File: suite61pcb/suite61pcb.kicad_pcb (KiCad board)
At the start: 2 copper layers, 176.3 x 113.1 mm, 99 parts, among them J1 Battery JST, J2 OLED, J3 FFC_Receiver, SW1 MX_SW_HS, SW10 MX_SW_HS, SW11 MX_SW_HS, SW12 MX_SW_HS, SW13 MX_SW, SW14 MX_SW, SW15 MX_SW_HS, SW16 MX_SW_HS, SW17 MX_SW_HS, SW18 MX_SW_HS, SW19 MX_SW_HS, SW2 MX_SW_HS, SW20 Reset_Button, SW21 MX_SW, SW22 MX_SW, SW23 MX_SW_HS, SW24 MX_SW_HS, SW25 MX_SW_HS, SW26 MX_SW_HS, SW27 MX_SW_HS, SW28 MX_SW_HS, SW29 MX_SW_HS, SW3 MX_SW_HS, SW30 MX_SW_HS, SW31 MX_SW_HS, SW32 MX_SW_HS, SW33 MX_SW_HS, SW34 MX_SW_HS, SW35 MX_SW_HS, SW36 MX_SW_HS, SW37 RotaryEncoder_Switch, SW4 MX_SW_HS, SW5 MX_SW_HS, SW6 MX_SW_HS, SW7 MX_SW_HS, SW8 MX_SW_HS, SW9 MX_SW_HS, U1 nice_nano

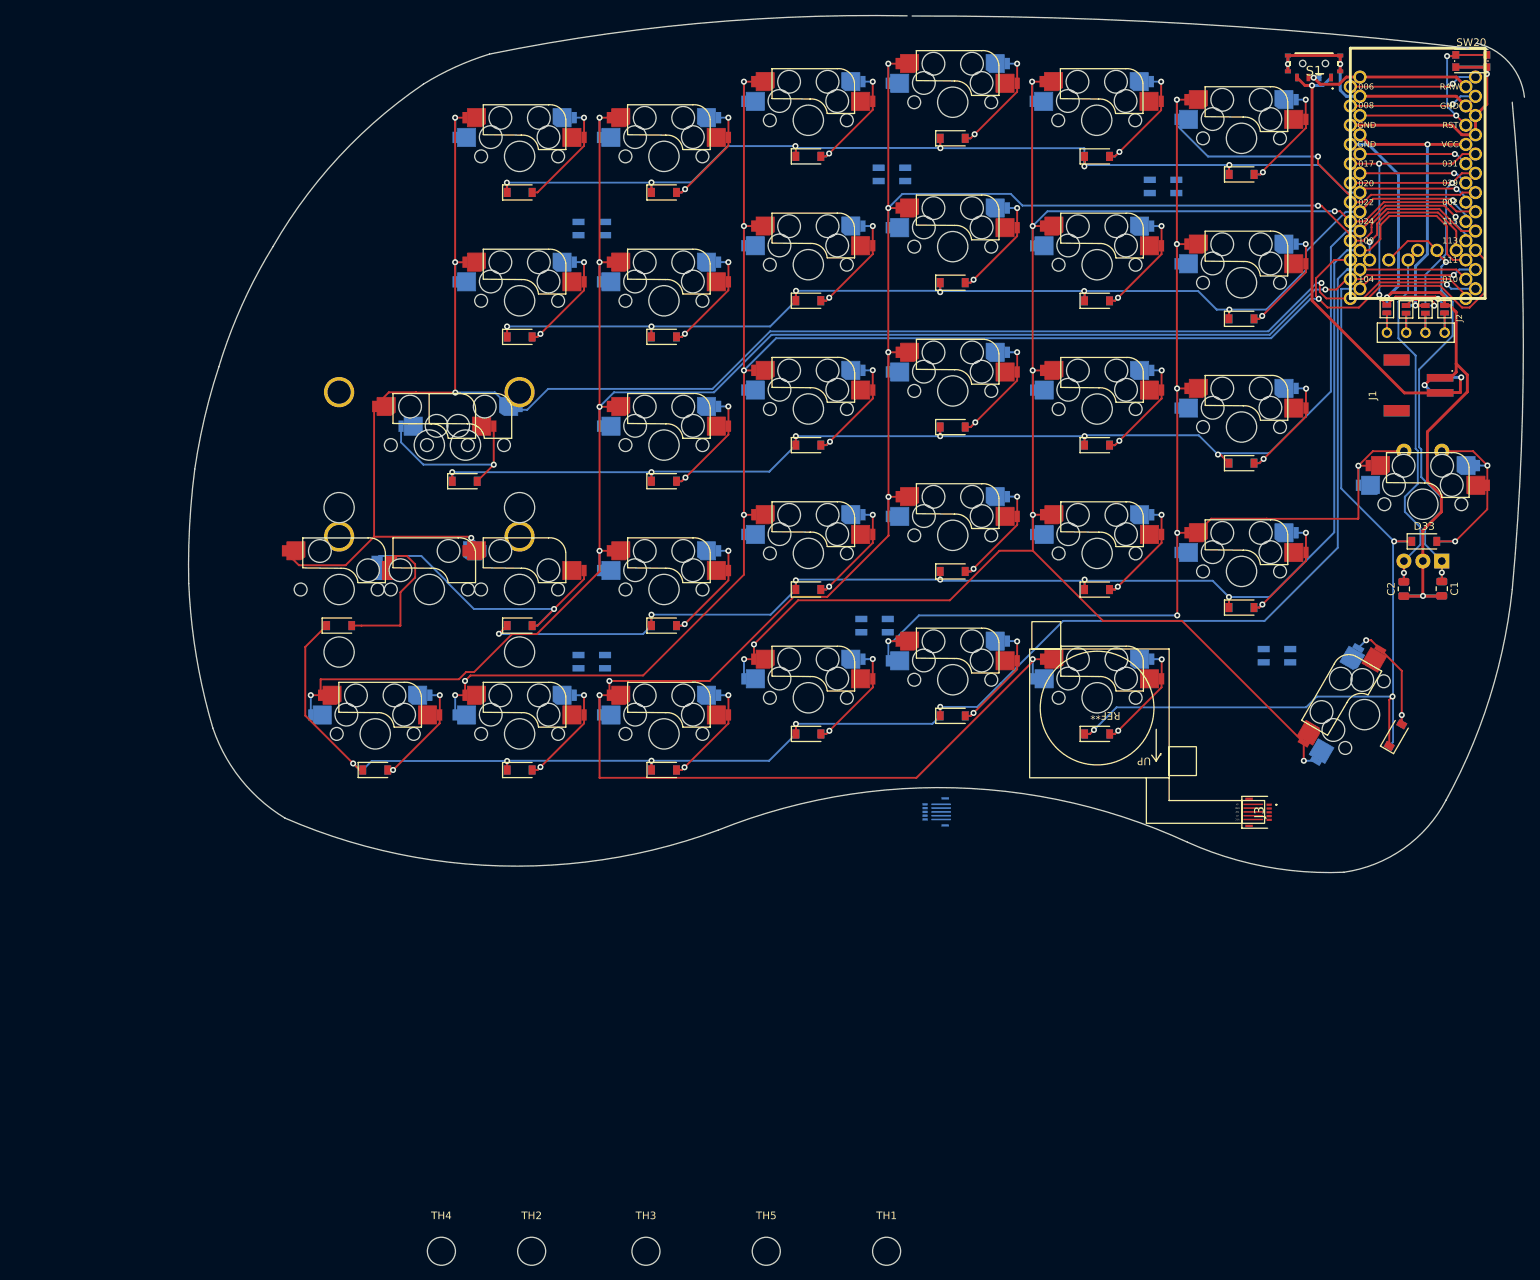
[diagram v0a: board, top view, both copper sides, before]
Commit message: finished routing pcb, look into possible trrs + magnetic connection between halves
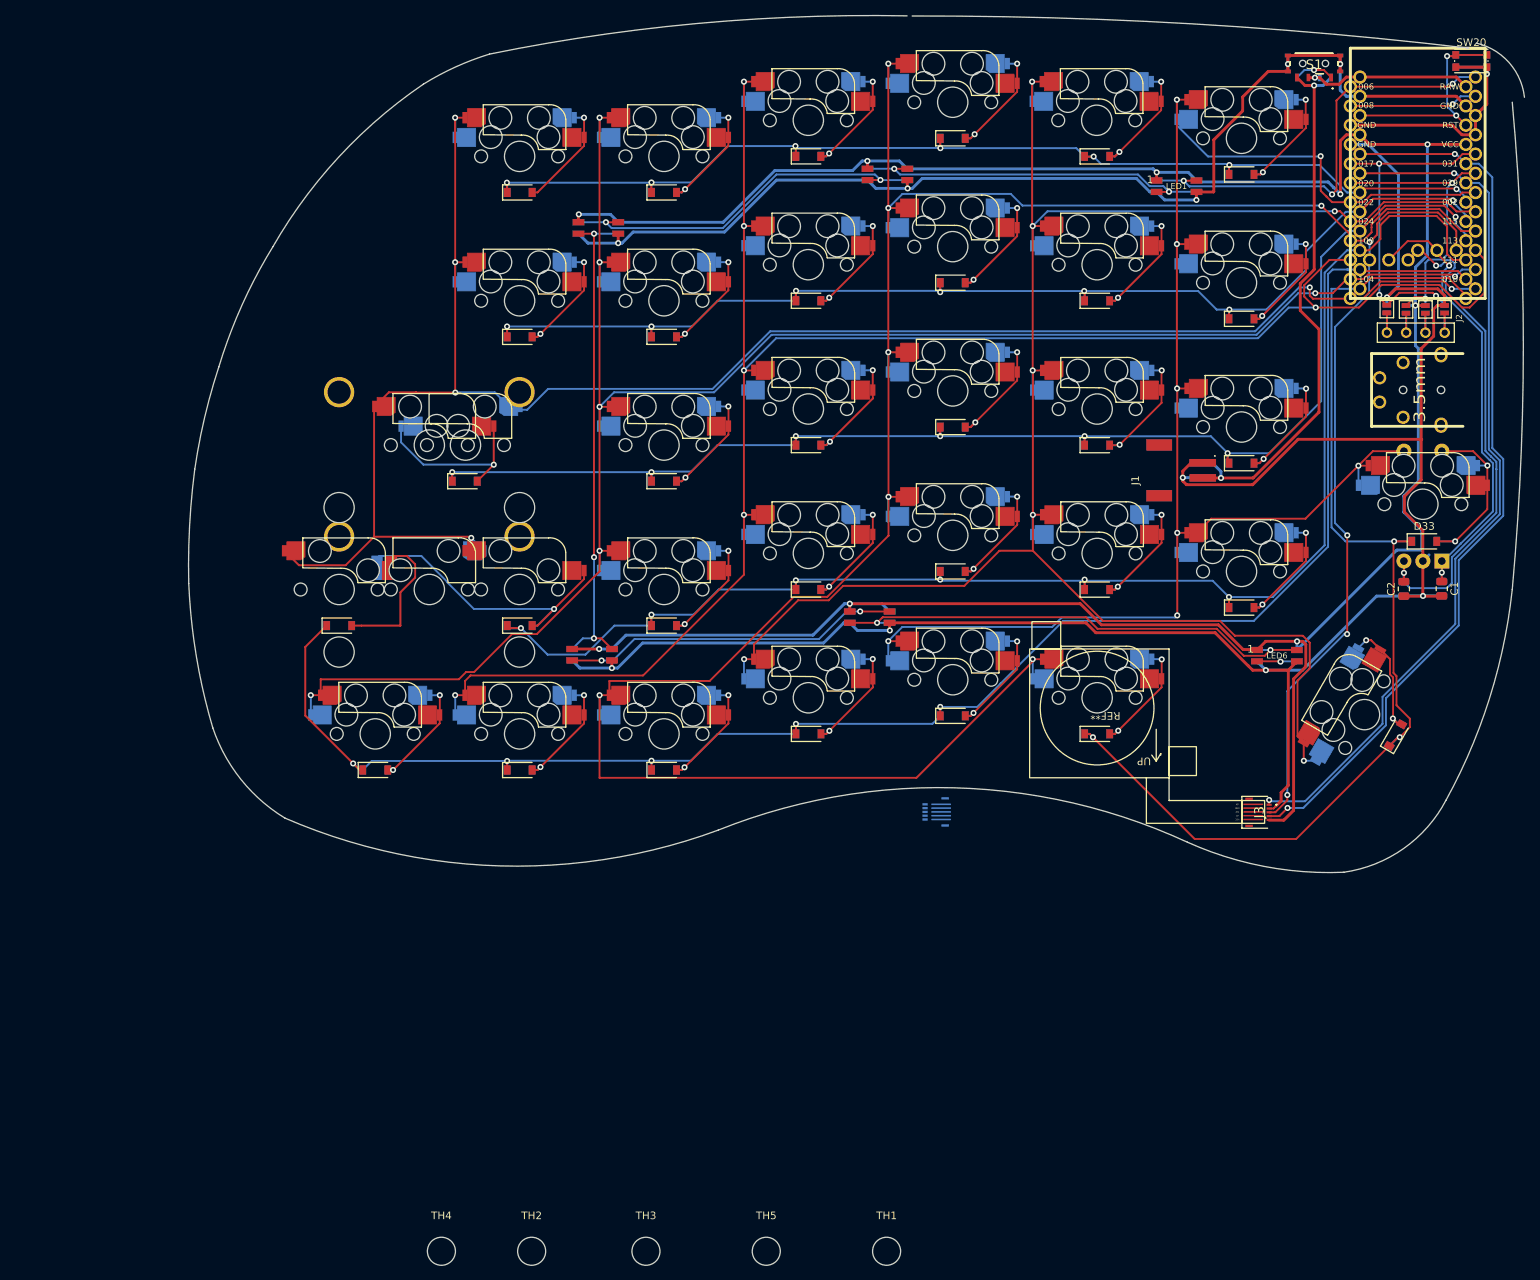
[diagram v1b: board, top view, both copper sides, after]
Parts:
- added J2: 3.5mm, Keebio-Parts:TRRS_Jack, F.Cu at (207.8, 71.3)
- LED1, LED6: footprint LED_SMD:LED_SK6812MINI_PLCC4_3.5x3.5mm_P1.75mm -> suite61:SK6812MINI-E; moved to F.Cu
- LED2, LED3, LED4, LED5: footprint LED_SMD:LED_SK6812MINI_PLCC4_3.5x3.5mm_P1.75mm -> suite61:SK6812MINI-E
- moved J1 33.3 mm to (181.4, 81.9)
- moved LED1 1.78 mm to (177.9, 44.4), turned to 0 degrees
- moved LED5 1.29 mm to (137.5, 101.3)
- moved LED4 0.92 mm to (100.8, 106.2)
- moved LED3 0.87 mm to (101.7, 49.9)
- moved LED2 0.58 mm to (139.8, 42.9)
- turned LED6 to 0 degrees
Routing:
- net VCC: track 39.0 -> 351.1 mm, vias 2 -> 9
- net GND: track 173.7 -> 468.3 mm, vias 6 -> 12
- net JSX: track 14.5 -> 118.4 mm, vias 1 -> 2
- net JSY: track 14.5 -> 115.0 mm, vias 1 -> 2
- net JSBTN: track 19.8 -> 100.5 mm, vias 1 -> 4
- net Net-(LED5-PadP$2): track 0.00 -> 65.3 mm, vias 0 -> 2
- net Net-(LED3-PadP$2): track 0.00 -> 65.0 mm, vias 0 -> 3
- net Net-(LED2-PadP$2): track 0.00 -> 50.3 mm, vias 0 -> 2
- net Net-(LED1-PadP$2): track 0.00 -> 48.1 mm, vias 0 -> 2
- net Net-(LED4-PadP$2): track 0.00 -> 44.6 mm, vias 0 -> 2
- net LED: track 17.0 -> 57.9 mm, vias 1 -> 3
- net Enc0: track 49.5 -> 66.8 mm, vias 1 -> 2
- net Net-(J1-Pad2): track 62.3 -> 74.2 mm
- net row5: track 137.5 -> 148.4 mm
- net col1: track 237.5 -> 247.0 mm, vias 8 -> 7
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
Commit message: routing & edge design
finished routing pcb, added LED off switch
drew edge design in illustrator subject to change
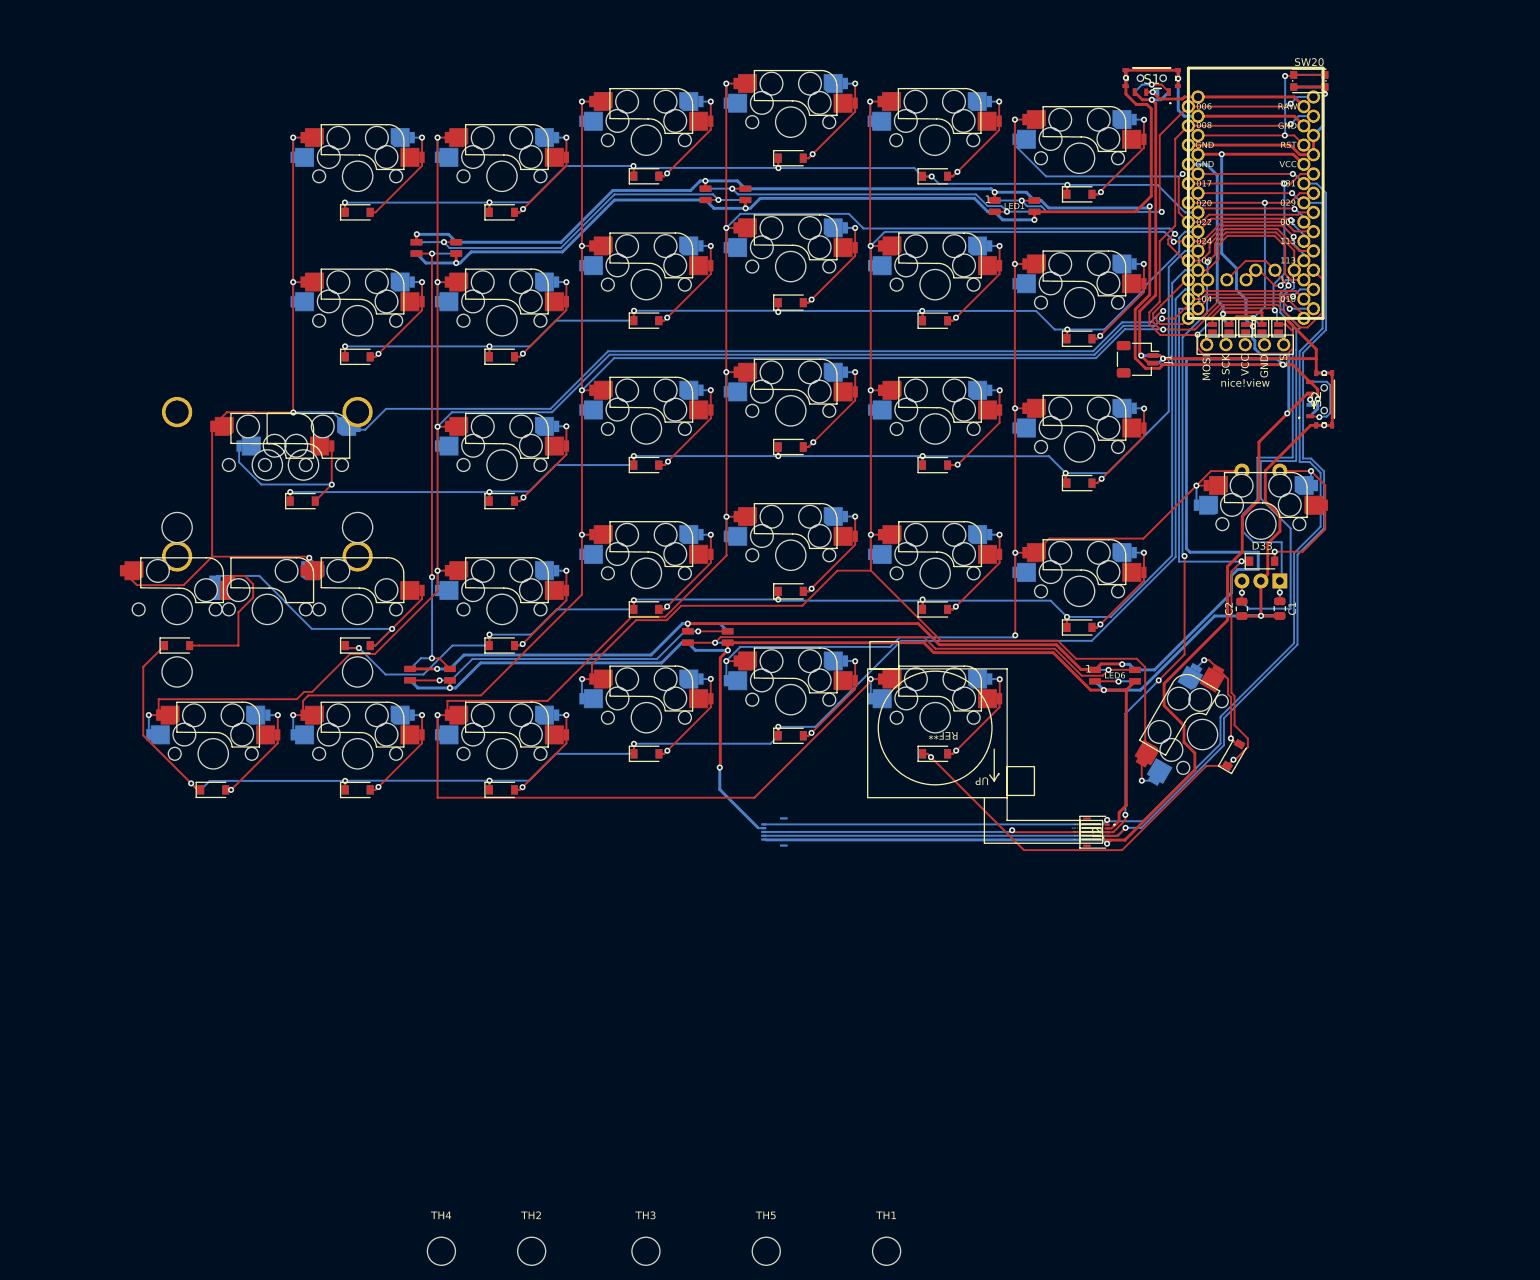
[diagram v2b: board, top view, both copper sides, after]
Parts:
- removed the J2 at (207.8, 71.3)
- removed the J2 at (213.3, 63.7)
- added Display1: nice!view, nice_view:nice_view, F.Cu at (187.0, 48.8)
- added JP1: Jumper_NO_Small, suite61:jumper, B.Cu at (183.6, 64.3)
- added JP10: Jumper_NO_Small, suite61:jumper, F.Cu at (190.5, 64.3)
- added S2: MSK12C02, LIB_MSK12C02:MSK12C02, F.Cu at (197.4, 72.5)
- J1: footprint suite61:JST_S2B-PH-SM4-TB -> suite61:JST_SH_SM02B-SRSS-TB_1x02-1MP_P1.00mm_Horizontal
- moved JP9 24.2 mm to (188.3, 64.3)
- moved JP8 23.9 mm to (186.2, 64.3)
- moved JP7 23.5 mm to (184.0, 64.3)
- moved JP6 23.2 mm to (181.8, 64.3)
- moved JP5 22.0 mm to (192.3, 64.3)
- moved JP4 21.7 mm to (190.1, 64.3)
- moved D10 21.5 mm to (127.1, 59.8)
- moved D16 21.5 mm to (127.1, 78.8)
- moved D22 21.5 mm to (127.1, 97.9)
- moved D4 21.5 mm to (127.1, 40.7)
- moved SW10 21.5 mm to (127.1, 55.0)
- moved SW4 21.5 mm to (127.1, 36.0)
- moved C1 21.5 mm to (191.6, 100.2)
- moved C2 21.5 mm to (186.6, 100.2)
- moved D1 21.5 mm to (69.9, 47.9)
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- renumbered J3 to J2, JP1 to JP2, JP2 to JP3, JP3 to JP4, JP4 to JP5, JP5 to JP6, JP6 to JP7, JP7 to JP8, JP8 to JP9
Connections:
- J2 pad 2: JSX -> JSY
- J2 pad 5: JSY -> JSX
- J3 pad 1: (no net) -> VCC
- J3 pad 2: (no net) -> JSY
- J3 pad 3: (no net) -> JSBTN
- J3 pad 4: (no net) -> GND
- J3 pad 5: (no net) -> JSX
- JP2 pad 1: Net-(J2-Pad4) -> Net-(Display1-Pad4)
- JP3 pad 1: Net-(J2-Pad3) -> Net-(Display1-Pad3)
- JP4 pad 1: Net-(J2-Pad2) -> Net-(Display1-Pad2)
- JP5 pad 1: Net-(J2-Pad1) -> Net-(Display1-Pad1)
- JP6 pad 1: Net-(J2-Pad4) -> Net-(Display1-Pad5)
- JP7 pad 1: Net-(J2-Pad3) -> Net-(Display1-Pad4)
- JP8 pad 1: Net-(J2-Pad2) -> Net-(Display1-Pad3)
- JP9 pad 1: Net-(J2-Pad1) -> Net-(Display1-Pad2)
- LED1 pad P$1: VCC -> LEDPWR
- LED2 pad P$1: VCC -> LEDPWR
- LED3 pad P$1: VCC -> LEDPWR
- LED4 pad P$1: VCC -> LEDPWR
- LED5 pad P$1: VCC -> LEDPWR
- LED6 pad P$1: VCC -> LEDPWR
- U1 pad 19: JSY -> JSX
- U1 pad 2: DATA -> DISPLAY
- U1 pad 20: JSX -> JSY
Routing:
- net LEDPWR: track 0.00 -> 337.6 mm, vias 0 -> 9
- net VCC: track 351.1 -> 179.7 mm, vias 9 -> 5
- net DISPLAY: track 0.00 -> 74.3 mm, vias 0 -> 2
- net JSY: track 115.0 -> 167.8 mm
- net JSBTN: track 100.5 -> 144.8 mm, vias 4 -> 5
- net JSX: track 118.4 -> 161.7 mm
- net Net-(J1-Pad2): track 74.2 -> 43.8 mm
- net GND: track 468.3 -> 498.4 mm, vias 12 -> 15
- net DATA: track 17.0 -> 0.00 mm, vias 1 -> 0
- net unconnected-(S2-PadA1): track 0.00 -> 9.45 mm, vias 0 -> 1
- net Net-(J2-Pad4): track 5.24 -> 0.00 mm
- net Net-(J2-Pad1): track 5.21 -> 0.00 mm
- net Net-(J2-Pad2): track 5.18 -> 0.00 mm
- net Net-(J2-Pad3): track 5.16 -> 0.00 mm
- net Enc1: track 59.5 -> 64.5 mm
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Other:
- board outline removed
- board text added: "battery: 123x43x1.5"
- board text added: "battery: 25x45x5.5"
- board text removed: "battery: 98x80x1.5"

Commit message: create pcb edge cut
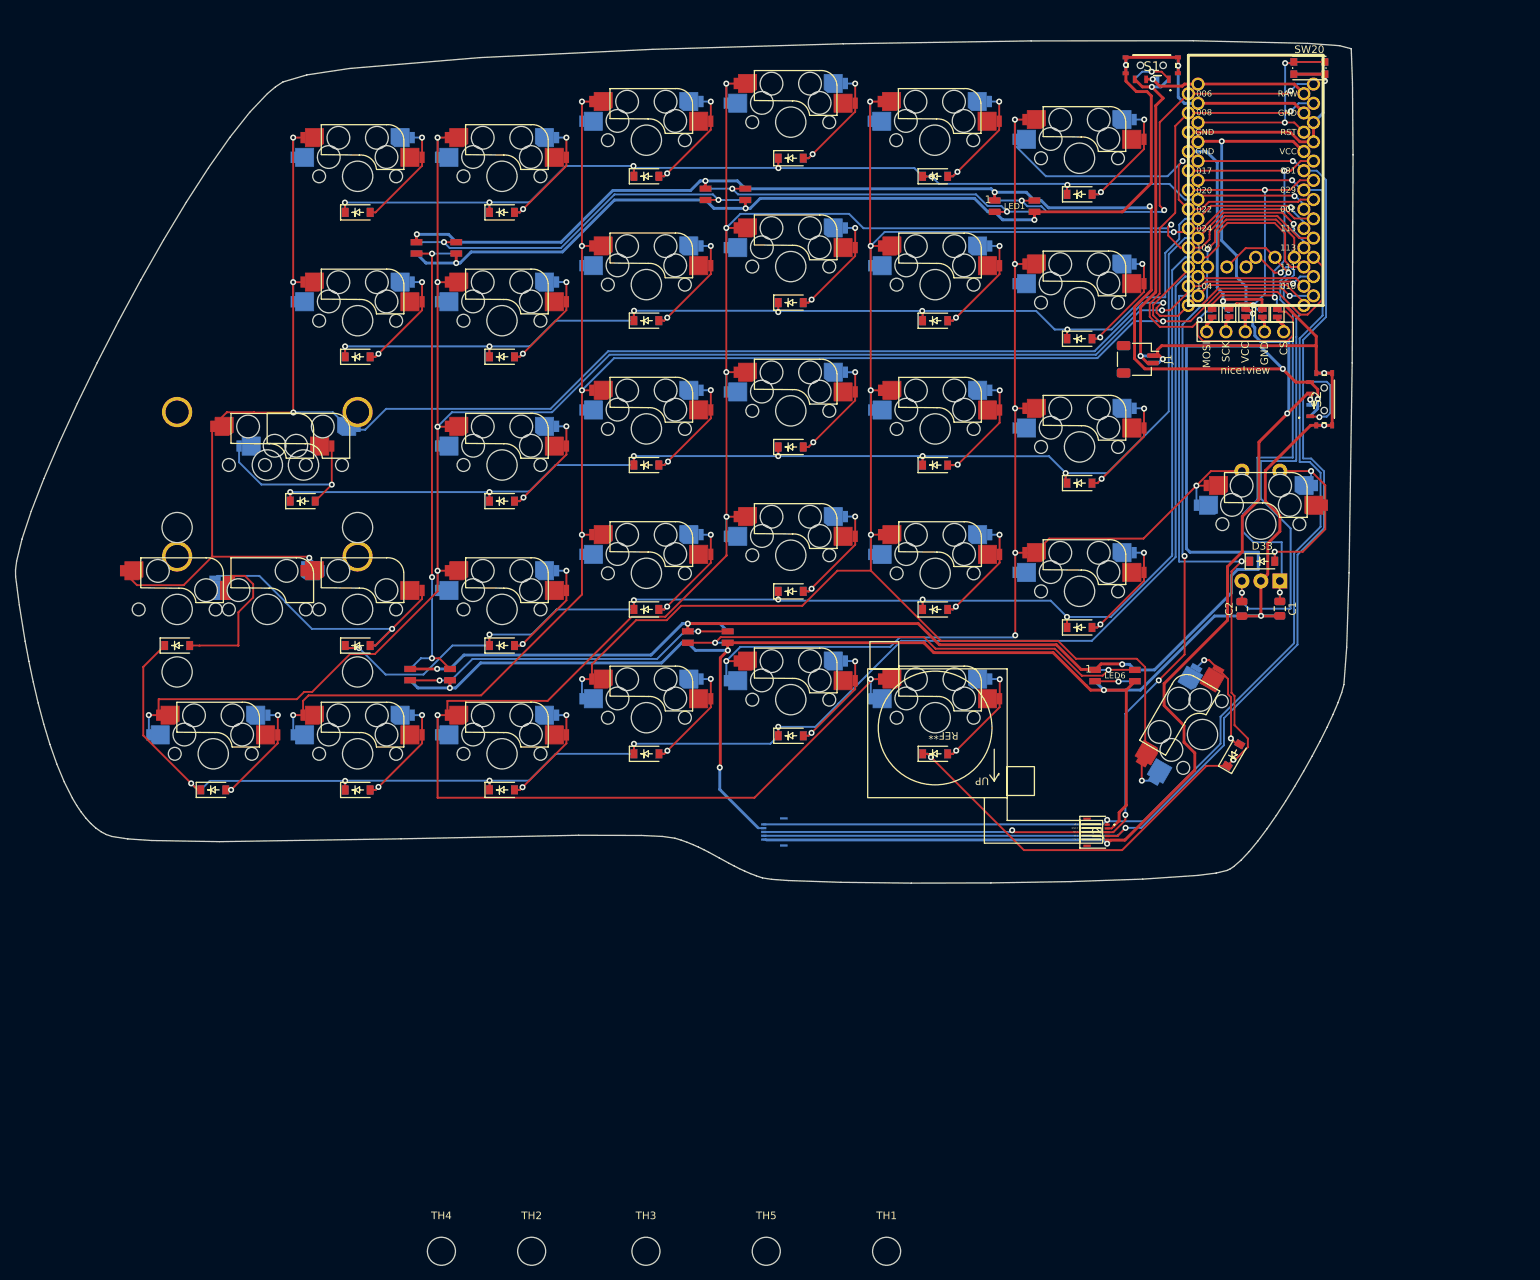
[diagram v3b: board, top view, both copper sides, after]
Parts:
- JP1, JP2, JP4, JP5: moved to F.Cu
- JP10, JP6, JP7, JP9: moved to B.Cu
- moved JP5 10.7 mm to (181.8, 62.3)
- moved JP6 10.5 mm to (192.1, 62.3)
- moved JP10 7.25 mm to (183.5, 62.3)
- moved JP1 7.07 mm to (190.4, 62.3)
- moved JP7 6.49 mm to (190.2, 62.3)
- moved JP4 6.46 mm to (184.0, 62.3)
- moved JP2 3.28 mm to (188.4, 62.3)
- moved JP9 3.27 mm to (185.8, 62.3)
- moved JP3 2.01 mm to (187.9, 62.3)
- moved JP8 2.01 mm to (186.2, 62.3)
- moved Display1 1.70 mm to (187.0, 47.1)
- moved U1 1.70 mm to (188.4, 44.9)
- moved S1 1.70 mm to (174.7, 28.5)
- moved SW20 1.70 mm to (195.5, 28.8)
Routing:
- net GND: track 498.4 -> 503.4 mm
- net Net-(Display1-Pad5): track 0.00 -> 4.00 mm
- net row1: track 153.9 -> 157.9 mm
- net Net-(Display1-Pad1): track 0.00 -> 3.88 mm
- net Net-(Display1-Pad2): track 0.00 -> 3.70 mm
- net Net-(Display1-Pad4): track 0.00 -> 3.51 mm
- net Net-(Display1-Pad3): track 0.00 -> 3.39 mm
- net LEDPWR: track 337.6 -> 340.0 mm
- net Net-(J1-Pad2): track 43.8 -> 46.2 mm
- net col2: track 295.1 -> 292.7 mm
- net JSX: track 161.7 -> 164.0 mm
- net LED: track 57.0 -> 59.0 mm
- net row3: track 195.0 -> 196.9 mm
- net Enc0: track 70.0 -> 71.7 mm
- net row4: track 227.4 -> 229.1 mm
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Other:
- board outline added: 176.5 x 111.1 mm
